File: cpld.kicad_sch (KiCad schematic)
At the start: 9 parts, among them J2 Conn_01x06_Pin, U6 ATF1508AS-10AU100

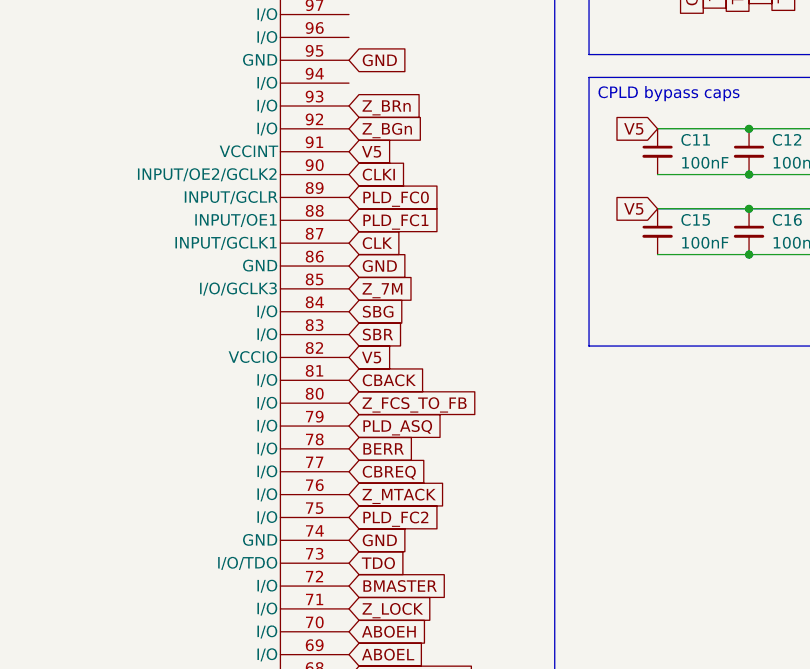
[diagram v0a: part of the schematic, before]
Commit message: Drop 74ABT74
The 74ABT74 is only used as a divider to create 25MHz from the 50MHz clock, and
it can be removed. Instead, the 50MHz are directly brought to the ATF1508. CLK
will be used as an output, not an input, so move away from GCLK pin. CLKI is no
longer needed on a pin as it doesn't connect to anything anymore.
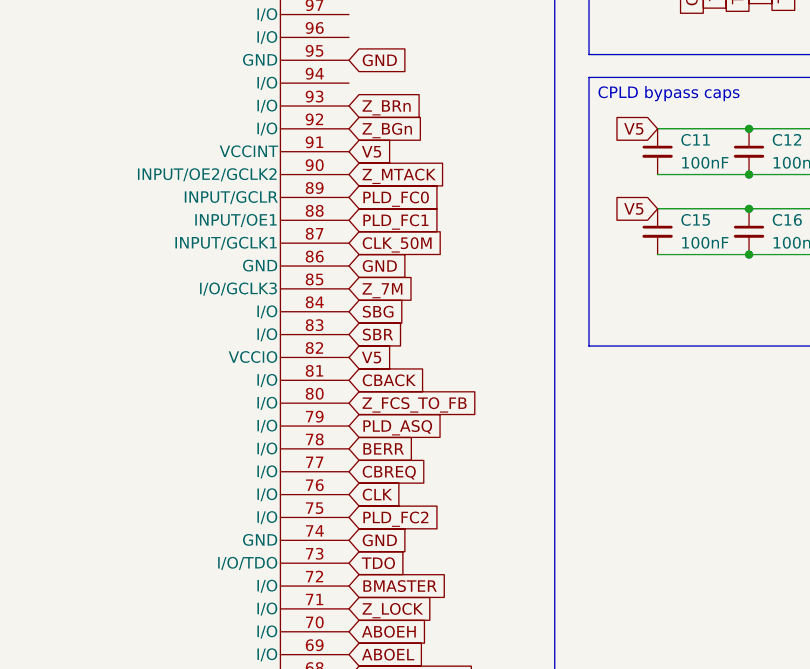
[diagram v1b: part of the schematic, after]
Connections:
- net CLKI is gone; now on net Z_MTACK: U6.90 (INPUT/OE2/GCLK2)
- net CLK: now also U6.76 (I/O); no longer U6.87 (INPUT/GCLK1)
- net Z_MTACK: no longer U6.76 (I/O)
- new net CLK_50M: U6.87 (INPUT/GCLK1)

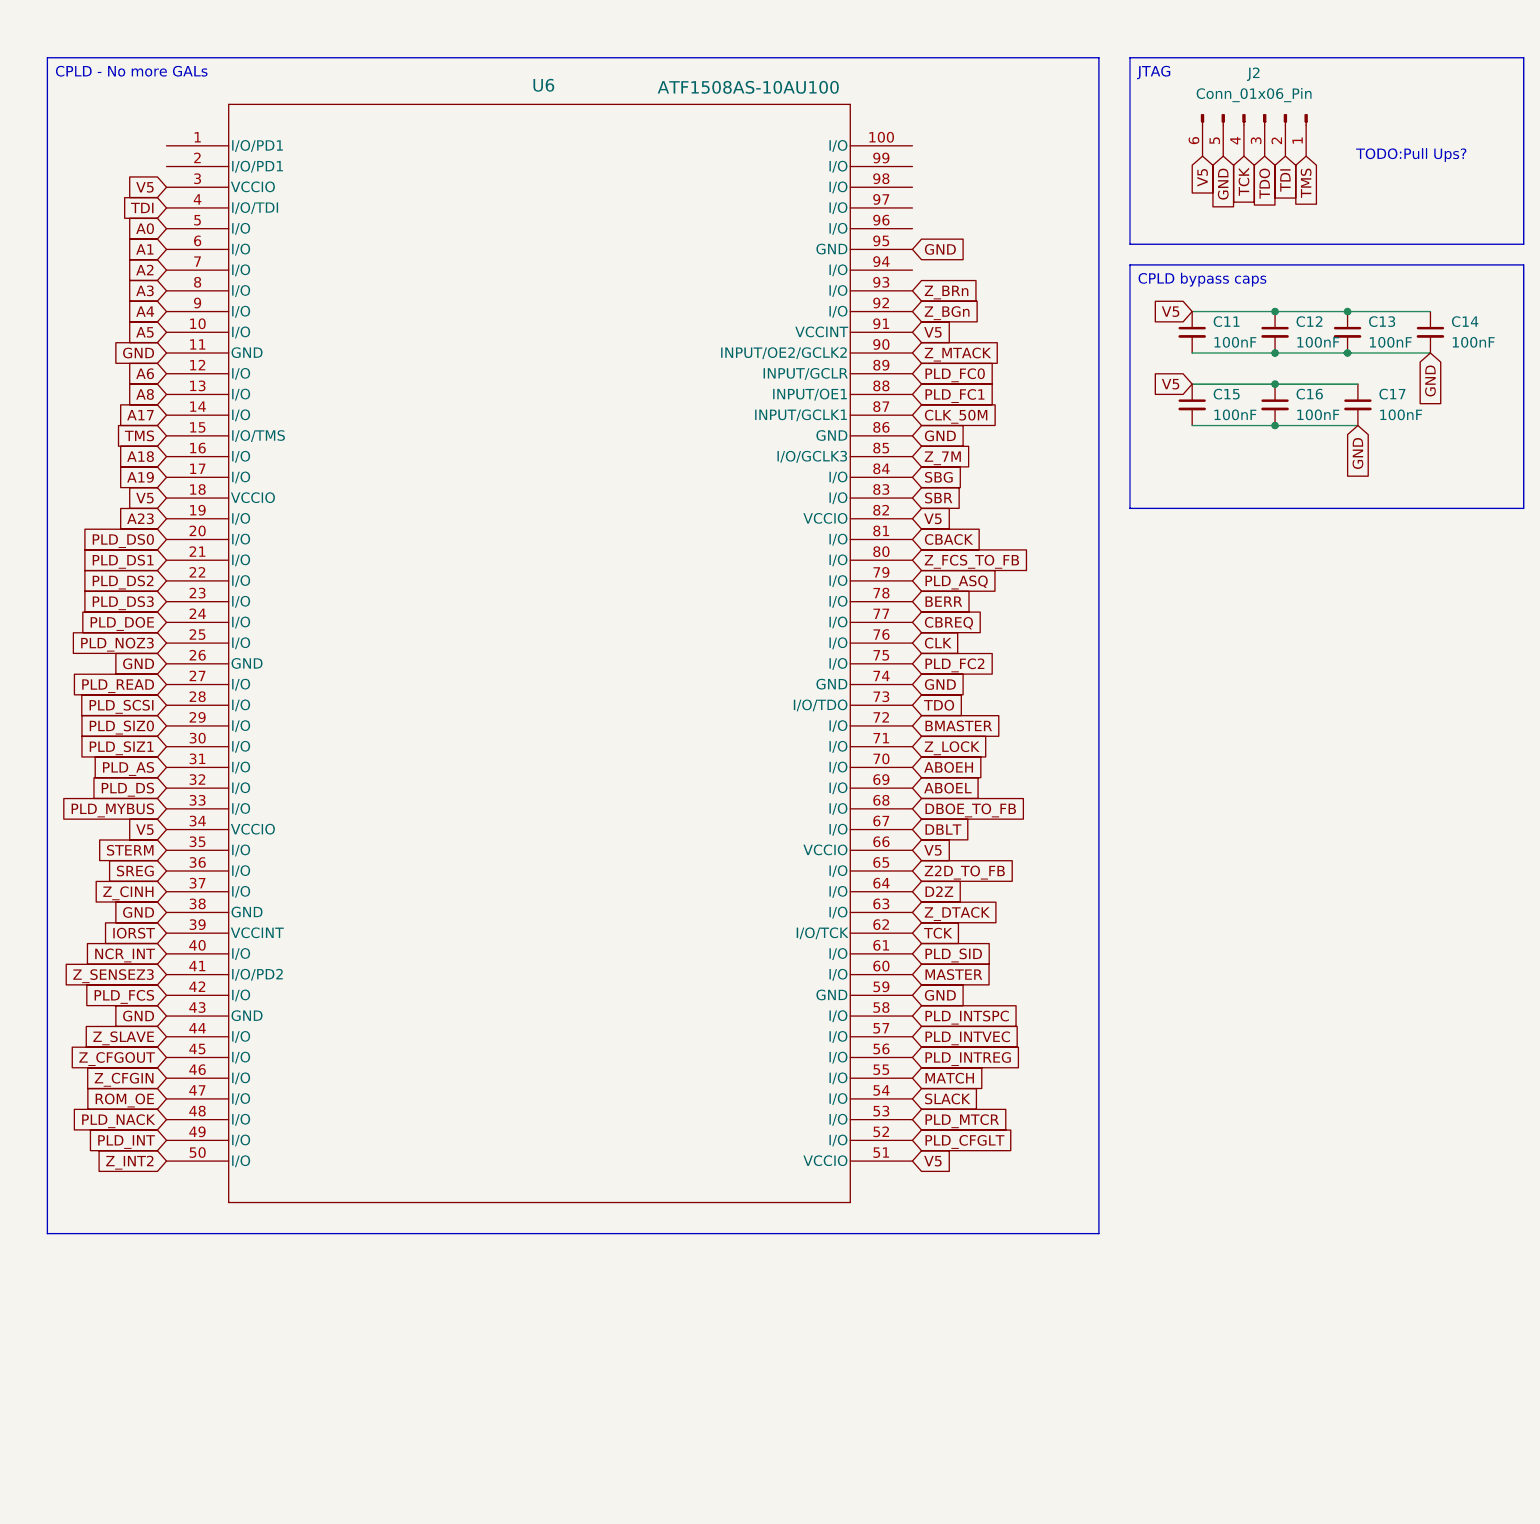
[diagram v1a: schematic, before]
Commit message: Move IORST to Reset / GCLR Pin
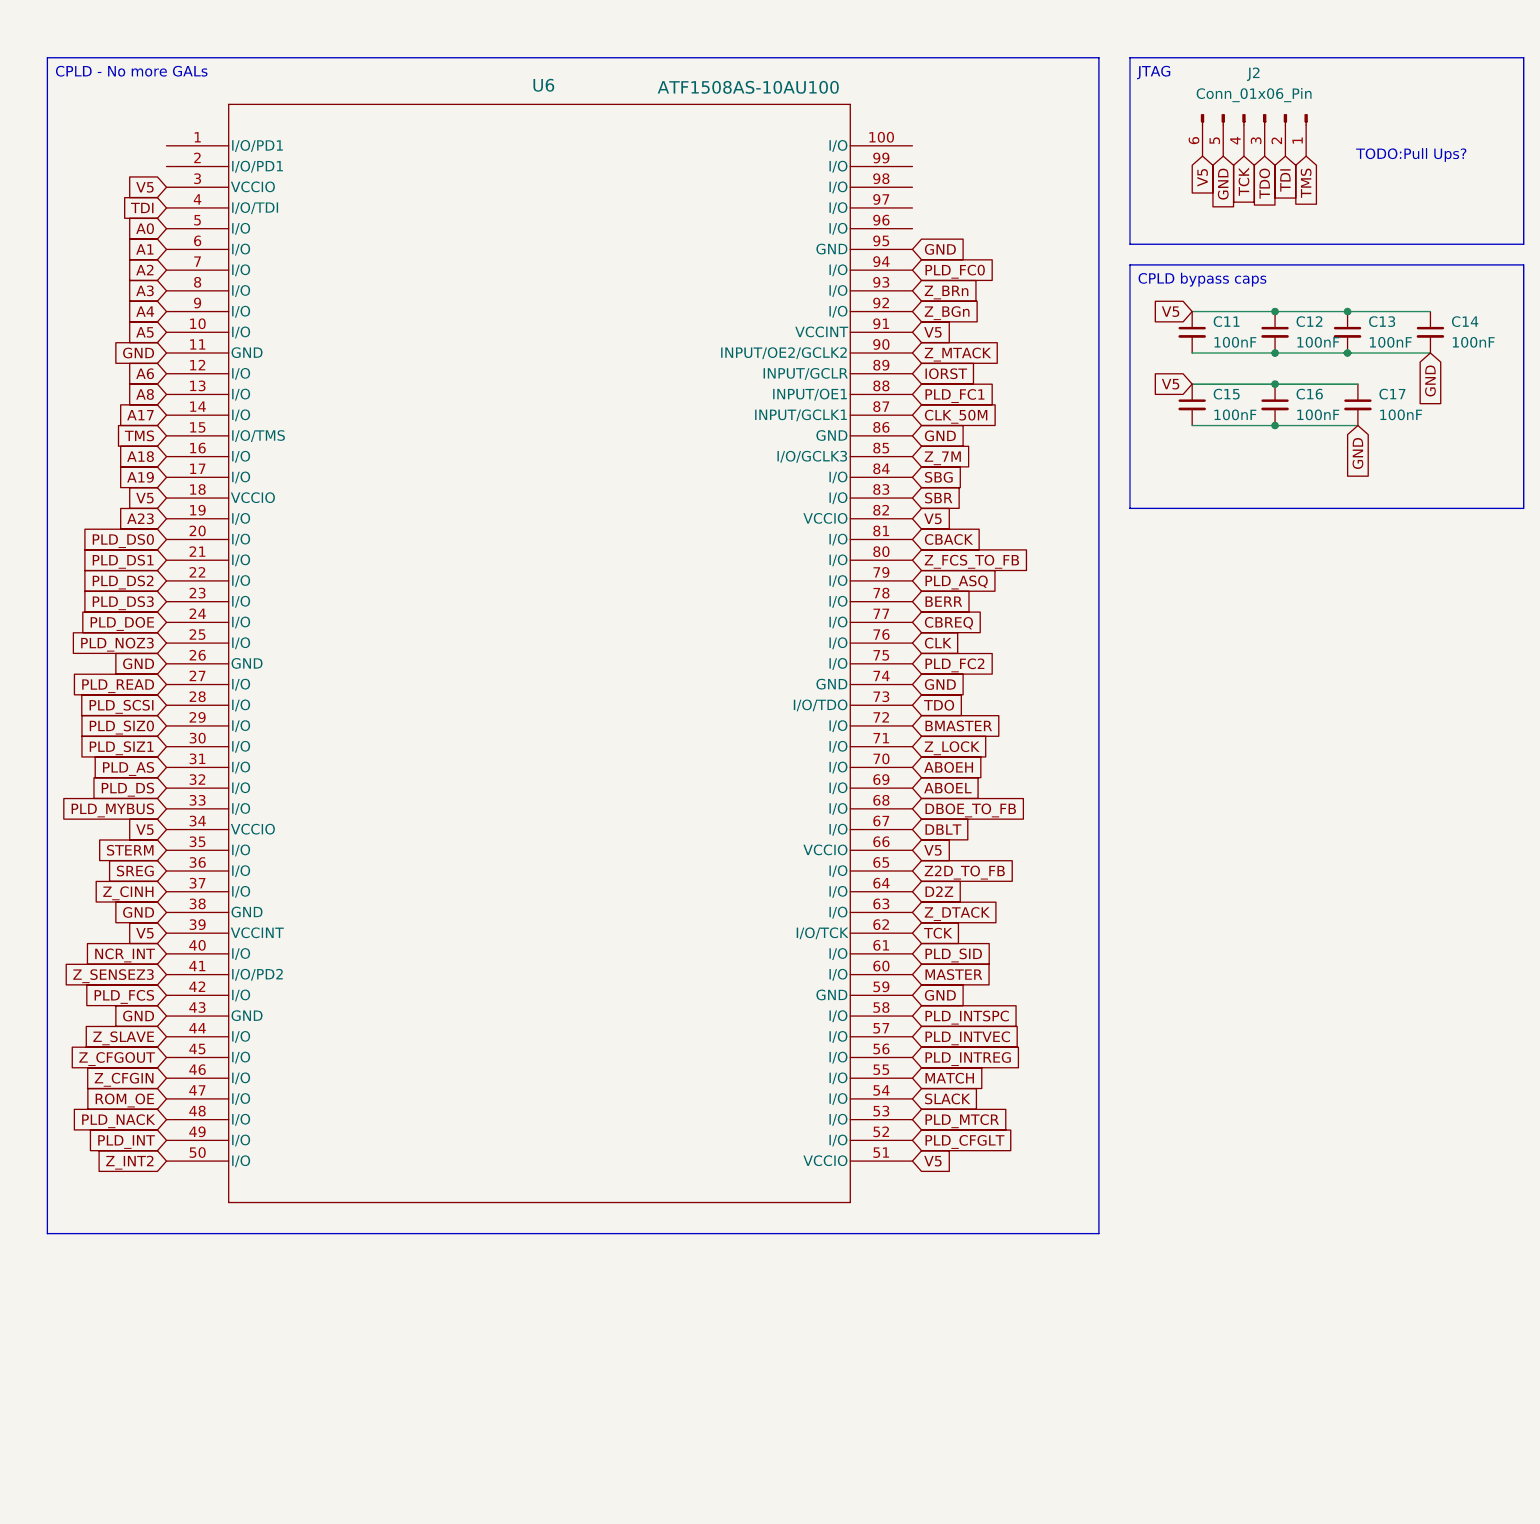
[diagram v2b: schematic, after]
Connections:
- net IORST: now also U6.89 (INPUT/GCLR); no longer U6.39 (VCCINT)
- net PLD_FC0: now also U6.94 (I/O); no longer U6.89 (INPUT/GCLR)
- net V5: now also U6.39 (VCCINT)

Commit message: Free up some pins and add an LED
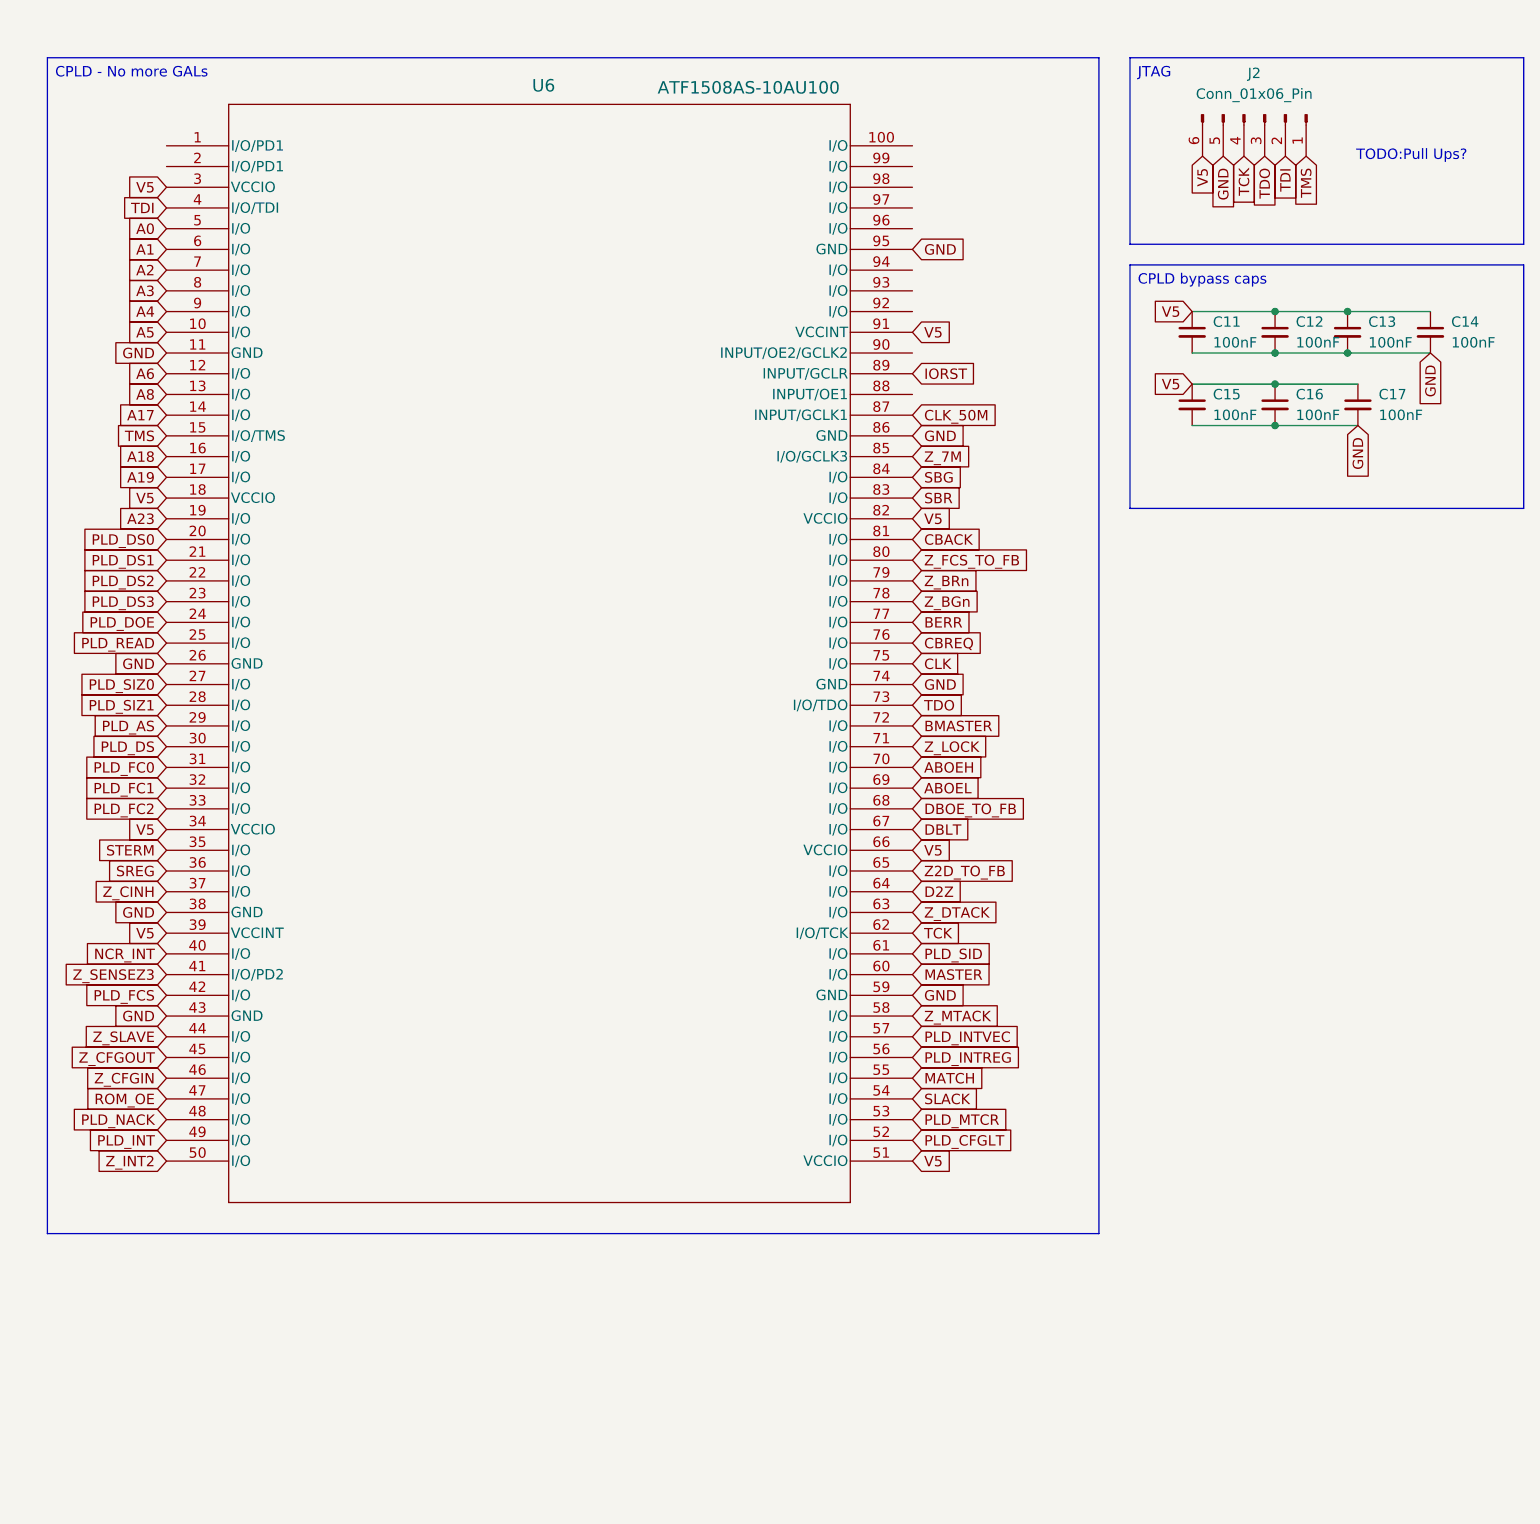
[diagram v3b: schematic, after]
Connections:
- net PLD_ASQ is gone; now on net Z_BRn: U6.79 (I/O)
- net PLD_INTSPC is gone; now on net Z_MTACK: U6.58 (I/O)
- net PLD_MYBUS is gone; now on net PLD_FC2: U6.33 (I/O)
- net PLD_NOZ3 is gone; now on net PLD_READ: U6.25 (I/O)
- net PLD_SCSI is gone; now on net PLD_SIZ1: U6.28 (I/O)
- net BERR: now also U6.77 (I/O); no longer U6.78 (I/O)
- net CBREQ: now also U6.76 (I/O); no longer U6.77 (I/O)
- net CLK: now also U6.75 (I/O); no longer U6.76 (I/O)
- net PLD_AS: now also U6.29 (I/O); no longer U6.31 (I/O)
- net PLD_DS: now also U6.30 (I/O); no longer U6.32 (I/O)
- net PLD_FC0: now also U6.31 (I/O); no longer U6.94 (I/O)
- net PLD_FC1: now also U6.32 (I/O); no longer U6.88 (INPUT/OE1)
- net PLD_FC2: no longer U6.75 (I/O)
- net PLD_READ: no longer U6.27 (I/O)
- net PLD_SIZ0: now also U6.27 (I/O); no longer U6.29 (I/O)
- net PLD_SIZ1: no longer U6.30 (I/O)
- net Z_BGn: now also U6.78 (I/O); no longer U6.92 (I/O)
- net Z_BRn: no longer U6.93 (I/O)
- net Z_MTACK: no longer U6.90 (INPUT/OE2/GCLK2)
